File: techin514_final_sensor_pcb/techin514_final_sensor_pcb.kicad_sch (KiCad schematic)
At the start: 9 parts, among them J1 28BYJ-48 Stepper Motor, SW1 CK_KMS2xxGP, U1 ESP32-C3-DevKitM-1, U2 ESP32-C3-DevKitM-1, U3 ADXL343, U4 ULN2003

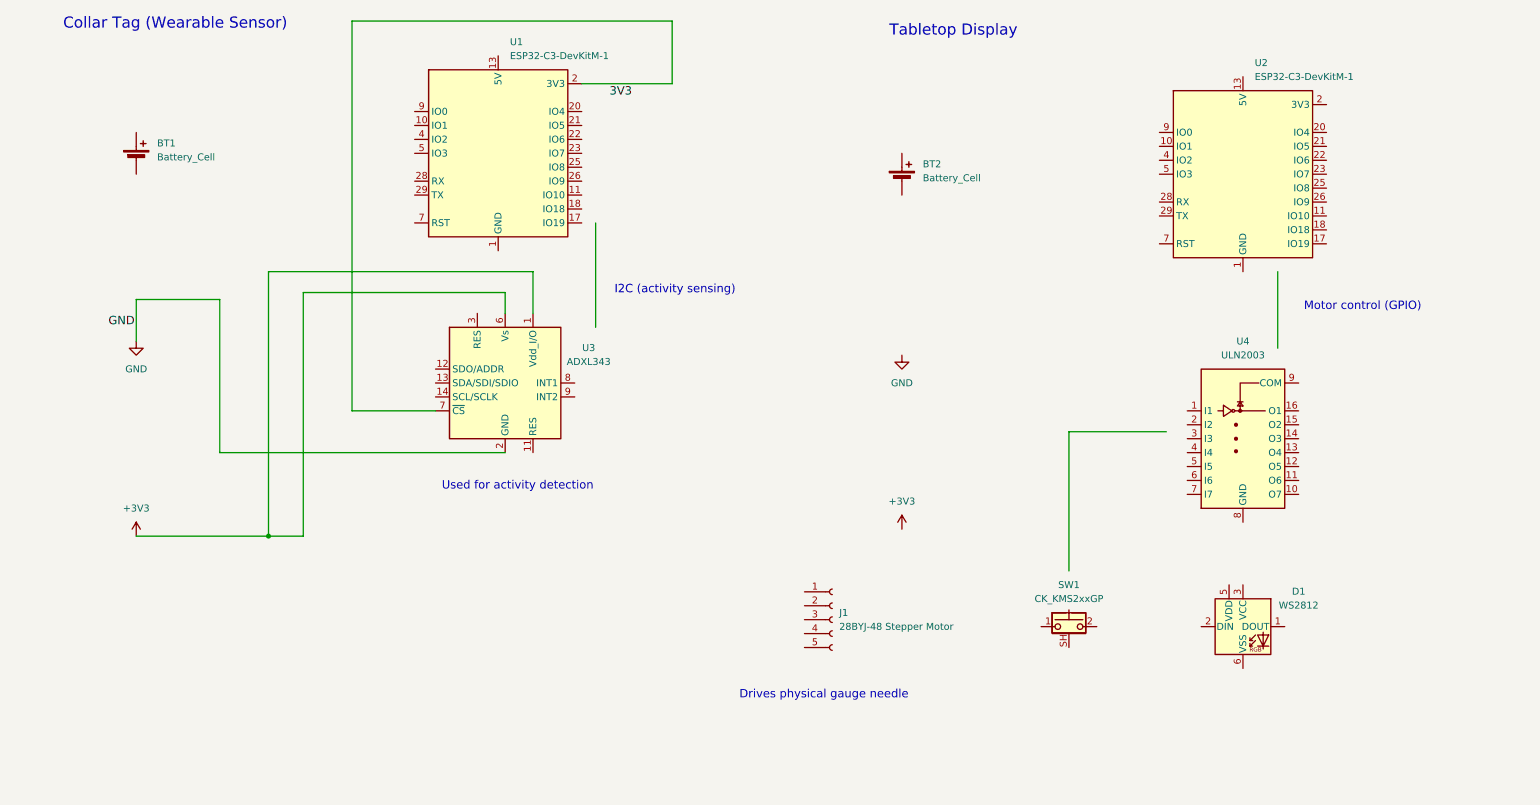
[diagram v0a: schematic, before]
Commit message: update schematic
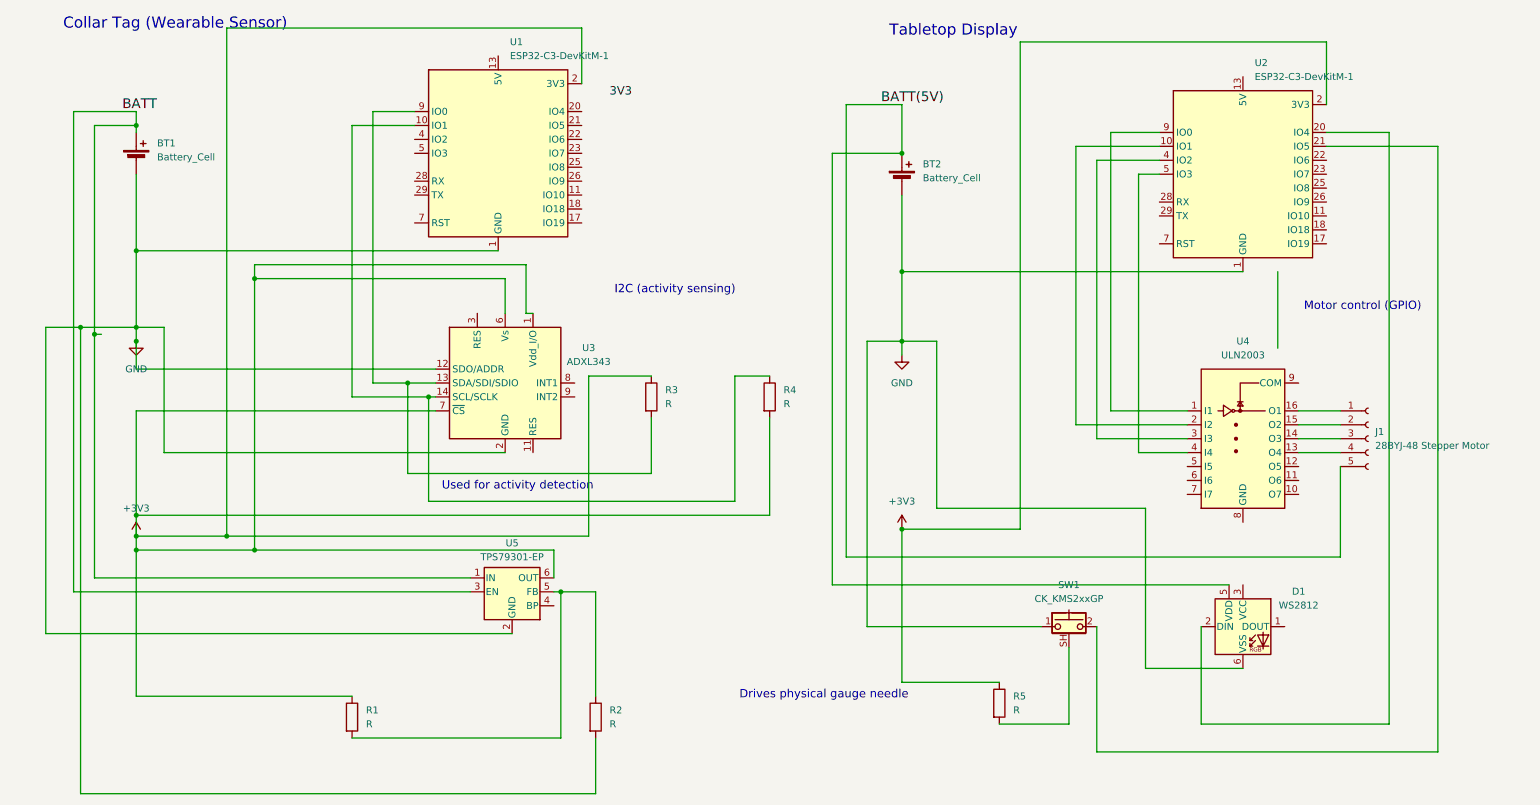
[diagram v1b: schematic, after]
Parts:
- added R1, R2, R3, R4, R5: R, symbol Device:R
- added U5: TPS79301-EP, Package_TO_SOT_SMD:SOT-23-6, symbol Regulator_Linear:TPS79301-EP
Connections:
- net +3V3: now also U1.2 (3V3), U1.3 (3V3), U2.2 (3V3), U2.3 (3V3), U3.7 (~{CS}), R1.1, R3.1, R4.2, R5.1, U5.6 (OUT)
- net GND: now also BT1.2 (-), BT2.2 (-), D1.6 (VSS), SW1.1, U1.1 (GND), U1.12 (GND), U1.15 (GND), U1.16 (GND), U1.19 (GND), U1.24 (GND), U1.27 (GND), U1.30 (GND), U1.6 (GND), U1.8 (GND), U2.1 (GND), U2.12 (GND), U2.15 (GND), U2.16 (GND), U2.19 (GND), U2.24 (GND), U2.27 (GND), U2.30 (GND), U2.6 (GND), U2.8 (GND), U3.12 (SDO/ADDR), R2.2, U5.2 (GND)
- net at U3.13 (SDA/SDI/SDIO): now also U1.9 (IO0), R3.2
- net at U3.14 (SCL/SCLK): now also U1.10 (IO1), R4.1
- net at U4.1 (I1): now also U2.9 (IO0)
- net at U4.13 (O4): now also J1.4 (Pin_4)
- net at U4.14 (O3): now also J1.3 (Pin_3)
- net at U4.15 (O2): now also J1.2 (Pin_2)
- net at U4.16 (O1): now also J1.1 (Pin_1)
- net at U4.2 (I2): now also U2.10 (IO1)
- net at U4.3 (I3): now also U2.4 (IO2)
- net at U4.4 (I4): now also U2.5 (IO3)
- net BATT(5V): now reaches BT2.1 (+)
- net BATT(5V): now also D1.5 (VDD), J1.5 (Pin_5)
- net at SW1.2: now also U2.21 (IO5)
- net at SW1.SH (B): now also R5.2
- net at D1.2 (DIN): now also U2.20 (IO4)
- net BATT: now reaches BT1.1 (+)
- net BATT: now also U5.1 (IN), U5.3 (EN)
- new net: R1.2, R2.1, U5.5 (FB)
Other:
- moved on the sheet: J1

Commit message: update schematic
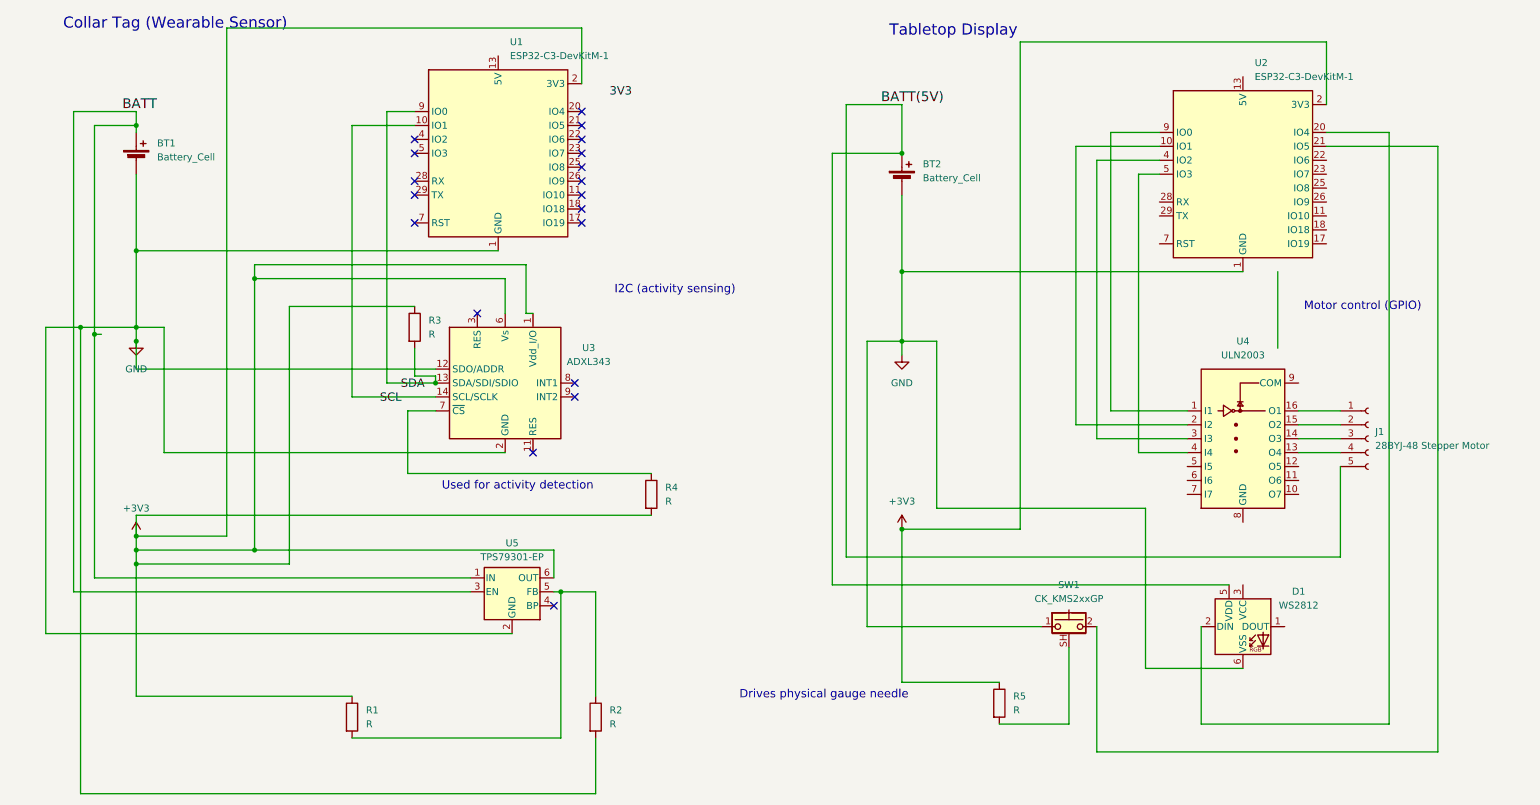
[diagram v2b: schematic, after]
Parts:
- BT1: footprint (none) -> Battery:BatteryHolder_Bulgin_BX0034_1xAAA
- BT2: footprint (none) -> Connector_PinHeader_1.00mm:PinHeader_1x02_P1.00mm_Vertical
- J1: footprint (none) -> Connector_PinHeader_1.00mm:PinHeader_1x05_P1.00mm_Vertical
- R1, R2, R3, R4, R5: footprint (none) -> Resistor_SMD:R_0603_1608Metric
- SW1: footprint Button_Switch_SMD:SW_SPST_CK_KMS2xxGP -> Button_Switch_SMD:SW_Push_1P1T-SH_NO_CK_KMR2xxG
- U4: footprint (none) -> Package_DIP:DIP-16_W7.62mm
- U5: footprint Package_TO_SOT_SMD:SOT-23-6 -> Package_SON:SON-8-1EP_3x2mm_P0.5mm_EP1.4x1.6mm
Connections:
- net +3V3: no longer U3.7 (~{CS})
- net at U1.10 (IO1), U3.14 (SCL/SCLK): no longer R4.1
- new net: R4.1, U3.7 (~{CS})
- no-connect marks 0 -> 19
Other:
- moved on the sheet: R3, R4

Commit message: update schematic and pcb
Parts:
- removed R5: R, Resistor_SMD:R_0603_1608Metric, symbol Device:R
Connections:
- net +3V3: no longer U2.2 (3V3), U2.3 (3V3)
- net BATT(5V): now also U2.13 (5V), U2.14 (5V)
- net GND: now also SW1.SH (B)
- new net: U2.2 (3V3), U2.3 (3V3)
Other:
- moved on the sheet: R1, R2, R4

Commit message: update pcb
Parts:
- removed U3: ADXL343, Package_LGA:LGA-14_3x5mm_P0.8mm_LayoutBorder1x6y, symbol Sensor_Motion:ADXL343
- added U6: LSM6DS3, Package_LGA:LGA-14_3x2.5mm_P0.5mm_LayoutBorder3x4y, symbol Sensor_Motion:LSM6DS3
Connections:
- net +3V3: now also R3.2, U6.12 (CS), U6.5 (VDDIO), U6.8 (VDD); no longer R3.1
- net GND: now also U6.1 (SDO/SA0), U6.6 (GND), U6.7 (GND)
- net at U1.9 (IO0): now also R3.1, U6.14 (SDA); no longer R3.2
- net at U1.10 (IO1): now also R4.1, U6.13 (SCL)
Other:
- moved on the sheet: R3, R4

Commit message: updated schematic and PCB
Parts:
- removed BT1: Battery_Cell, Battery:BatteryHolder_Bulgin_BX0034_1xAAA, symbol Device:Battery_Cell
- removed BT2: Battery_Cell, Connector_PinHeader_1.00mm:PinHeader_1x02_P1.00mm_Vertical, symbol Device:Battery_Cell
- removed D1: WS2812, LED_SMD:LED_WS2812_PLCC6_5.0x5.0mm_P1.6mm, symbol LED:WS2812
- removed J1: 28BYJ-48 Stepper Motor, Connector_PinHeader_1.00mm:PinHeader_1x05_P1.00mm_Vertical, symbol Connector:Conn_01x05_Socket
- removed R1, R2: R, Resistor_SMD:R_0603_1608Metric, symbol Device:R
- removed SW1: CK_KMS2xxGP, Button_Switch_SMD:SW_Push_1P1T-SH_NO_CK_KMR2xxG, symbol Switch:CK_KMS2xxGP
- removed U1, U2: ESP32-C3-DevKitM-1, RF_Module:ESP32-C3-DevKitM-1, symbol RF_Module:ESP32-C3-DevKitM-1
- removed U4: ULN2003, Package_DIP:DIP-16_W7.62mm, symbol Transistor_Array:ULN2003
- removed U5: TPS79301-EP, Package_SON:SON-8-1EP_3x2mm_P0.5mm_EP1.4x1.6mm, symbol Regulator_Linear:TPS79301-EP
- removed U6: LSM6DS3, Package_LGA:LGA-14_3x2.5mm_P0.5mm_LayoutBorder3x4y, symbol Sensor_Motion:LSM6DS3
- added J1: J_BAT2, Connector_PinHeader_2.54mm:PinHeader_1x02_P2.54mm_Vertical, symbol Connector:Conn_01x02_Pin
- added J10: J_PWR2, Connector_PinHeader_2.54mm:PinHeader_1x04_P2.54mm_Vertical, symbol Connector:Conn_01x04_Pin
- added J2: J_BAT, Connector_PinHeader_2.54mm:PinHeader_1x02_P2.54mm_Vertical, symbol Connector:Conn_01x02_Pin
- added J3: J_ULN_IN, Connector_PinHeader_2.54mm:PinHeader_1x04_P2.54mm_Vertical, symbol Connector:Conn_01x04_Pin
- added J4: J_LDO, Connector_PinHeader_2.54mm:PinHeader_1x02_P2.54mm_Vertical, symbol Connector:Conn_01x03_Pin
- added J5: J_MOTOR, Connector_PinHeader_2.54mm:PinHeader_1x05_P2.54mm_Vertical, symbol Connector:Conn_01x05_Pin
- added J6: J_IMU, Connector_PinHeader_2.54mm:PinHeader_1x04_P2.54mm_Vertical, symbol Connector:Conn_01x04_Pin
- added J7: J_PWR, Connector_PinHeader_2.54mm:PinHeader_1x02_P2.54mm_Vertical, symbol Connector:Conn_01x04_Pin
- added J8: J_LED, Connector_PinHeader_2.54mm:PinHeader_1x03_P2.54mm_Vertical, symbol Connector:Conn_01x03_Pin
- added J9: J_SW, Connector_PinHeader_2.54mm:PinHeader_1x02_P2.54mm_Vertical, symbol Connector:Conn_01x02_Pin
- added U1, U2: ~, ESP32footprint:XIAO_ESP32, symbol GIX_ESP32:XIAO_ESP32
- R3, R4: footprint Resistor_SMD:R_0603_1608Metric -> Resistor_THT:R_Axial_DIN0207_L6.3mm_D2.5mm_P7.62mm_Horizontal
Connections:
- net at R4.1: now also J6.4 (SCL), U1.6 (GPIO6_A5_D5_SCL)
- net at R3.1: now also J6.3 (SDA), U1.5 (GPIO4_A3_D3_SDA)
- net +3V3: no longer names the net of R3.2, R4.2
- net +3V3: now also J4.2 (3V3), J6.1 (3V3), J7.1 (3V3), J7.3 (3V3), U1.12 (3V3)
- new net: J1.1 (VBAT_5V), J10.1 (3V3), J3.1 (MOTOR_IN1), U2.1 (GPIO1_A0_D0)
- new net: J1.2 (GND), J10.2 (GND), J3.2 (MOTOR_IN2), U2.2 (GPIO2_A1_D1)
- new net: J10.3 (3V3), J3.3 (MOTOR_IN3), U2.3 (GPIO3_A2_D2)
- new net: J10.4 (GND), J3.4 (Pin_4), U2.4 (GPIO4_A3_D3)
- new net: J8.3 (LED_DIN), U2.11 (GPIO9_A10_D10_COPI)
- new net: J6.2 (GND), J7.2 (GND), J7.4 (GND), U1.13 (GND)
- new net: J9.2 (Pin_2), U2.10 (GPIO8_A9_D9_CIPO)
- new net: J9.1 (BTN), U2.9 (GPIO7_A8_D8_SCK)
- new net: J2.1 (VBAT), J4.1 (VBAT), U1.15 (+BATT)
- new net: J2.2 (GND), J4.3 (GND), U1.16 (-BATT)
- no-connect marks 19 -> 0
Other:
- note removed: "I2C (activity sensing)"
- note removed: "Motor control (GPIO)"
- note removed: "Used for activity detection"

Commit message: updated PCB
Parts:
- removed J10: J_PWR2, Connector_PinHeader_2.54mm:PinHeader_1x04_P2.54mm_Vertical, symbol Connector:Conn_01x04_Pin
- removed J3: J_ULN_IN, Connector_PinHeader_2.54mm:PinHeader_1x04_P2.54mm_Vertical, symbol Connector:Conn_01x04_Pin
- removed J8: J_LED, Connector_PinHeader_2.54mm:PinHeader_1x03_P2.54mm_Vertical, symbol Connector:Conn_01x03_Pin
- removed J9: J_SW, Connector_PinHeader_2.54mm:PinHeader_1x02_P2.54mm_Vertical, symbol Connector:Conn_01x02_Pin
- added BT1: Battery_Cell, Connector_JST:JST_PH_B2B-PH-K_1x02_P2.00mm_Vertical, symbol Device:Battery_Cell
- added D1: LED, LED_SMD:LED_0603_1608Metric, symbol Device:LED
- added R1: R, Resistor_SMD:R_0603_1608Metric, symbol Device:R
- added U3: ULN2003, Package_SO:SOIC-16_3.9x9.9mm_P1.27mm, symbol Transistor_Array:ULN2003
- J1: value J_BAT2 -> SW1
- R3, R4: value R -> 4.7kOhm; footprint Resistor_THT:R_Axial_DIN0207_L6.3mm_D2.5mm_P7.62mm_Horizontal -> Resistor_SMD:R_0603_1608Metric
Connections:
- net at U2.1 (GPIO1_A0_D0): now also U3.1 (I1); no longer J1.1 (VBAT_5V)
- net at U2.2 (GPIO2_A1_D1): now also U3.2 (I2); no longer J1.2 (GND)
- net at U2.3 (GPIO3_A2_D2): now also U3.3 (I3)
- net at U2.4 (GPIO4_A3_D3): now also U3.4 (I4)
- net at U2.11 (GPIO9_A10_D10_COPI): now also J1.1 (Pin_1)
- net at J5.1 (COIL_A): now also U3.16 (O1)
- net at J5.2 (COIL_B): now also U3.15 (O2)
- net at J5.3 (COIL_C): now also U3.14 (O3)
- net at J5.4 (COIL_D): now also U3.13 (O4)
- net at J5.5 (V_MOTOR): now also U2.15 (+BATT), BT1.1 (+), U3.9 (COM)
- net at U2.10 (GPIO8_A9_D9_CIPO): now also R1.2
- net GND: now reaches U2.13 (GND)
- net GND: now also J1.2 (Pin_2), BT1.2 (-), D1.1 (K)
- new net: D1.2 (A), R1.1
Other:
- note removed: "Drives physical gauge needle"
- company: TECHIN514 -> TECHIN514 - Mengqi Shi
- moved on the sheet: J2, J4, J5, J6, J7, R3, R4, U1, U2

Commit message: update code
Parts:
- removed J2: J_BAT, Connector_PinHeader_2.54mm:PinHeader_1x02_P2.54mm_Vertical, symbol Connector:Conn_01x02_Pin
- removed J4: J_LDO, Connector_PinHeader_2.54mm:PinHeader_1x02_P2.54mm_Vertical, symbol Connector:Conn_01x03_Pin
- removed J6: J_IMU, Connector_PinHeader_2.54mm:PinHeader_1x04_P2.54mm_Vertical, symbol Connector:Conn_01x04_Pin
- removed J7: J_PWR, Connector_PinHeader_2.54mm:PinHeader_1x02_P2.54mm_Vertical, symbol Connector:Conn_01x04_Pin
- added BT3: Battery_Cell, symbol Device:Battery_Cell
- added SW1: SW_SPDT, Connector_PinHeader_2.54mm:PinHeader_1x03_P2.54mm_Vertical, symbol Switch:SW_SPDT
- added U4: LSM6DS3, Connector_PinHeader_2.54mm:PinHeader_1x05_P2.54mm_Vertical, symbol Sensor_Motion:LSM6DS3
- added U5: MCP1700x-330xxTO, Connector_PinHeader_2.54mm:PinHeader_1x03_P2.54mm_Vertical, symbol Regulator_Linear:MCP1700x-330xxTO
- J1: footprint Connector_PinHeader_2.54mm:PinHeader_1x02_P2.54mm_Vertical -> Button_Switch_THT:SW_Slide-03_Wuerth-WS-SLTV_10x2.5x6.4_P2.54mm
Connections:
- net GND: now also U1.13 (GND), U4.6 (GND), U4.7 (GND), U5.1 (GND)
- net +3V3: now reaches R3.2, R4.2
- net +3V3: now also U4.12 (CS), U4.5 (VDDIO), U4.8 (VDD), U5.3 (VO); no longer U1.12 (3V3)
- net at R3.1: now also U4.13 (SCL); no longer U1.5 (GPIO4_A3_D3_SDA)
- net at R4.1: now also U4.14 (SDA); no longer U1.6 (GPIO6_A5_D5_SCL)
- new net: SW1.2 (B), U5.2 (VI)
- new net +BATT: BT3.1 (+), SW1.1 (A)
- new net -BATT: BT3.2 (-), SW1.3 (C)
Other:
- moved on the sheet: R3, R4, U1
